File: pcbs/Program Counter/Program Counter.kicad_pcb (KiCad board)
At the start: 2 copper layers, 172.7 x 185.4 mm, 56 parts, among them J1001 Conn_02x20_Odd_Even, J1002 Conn_02x20_Odd_Even, U2001 74HC245, U2002 74HC245, U3001 74HC245, U3002 74HC245, U4001 74HC245, U4002 74HC245, U5001 74HC245, U5002 74HC245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

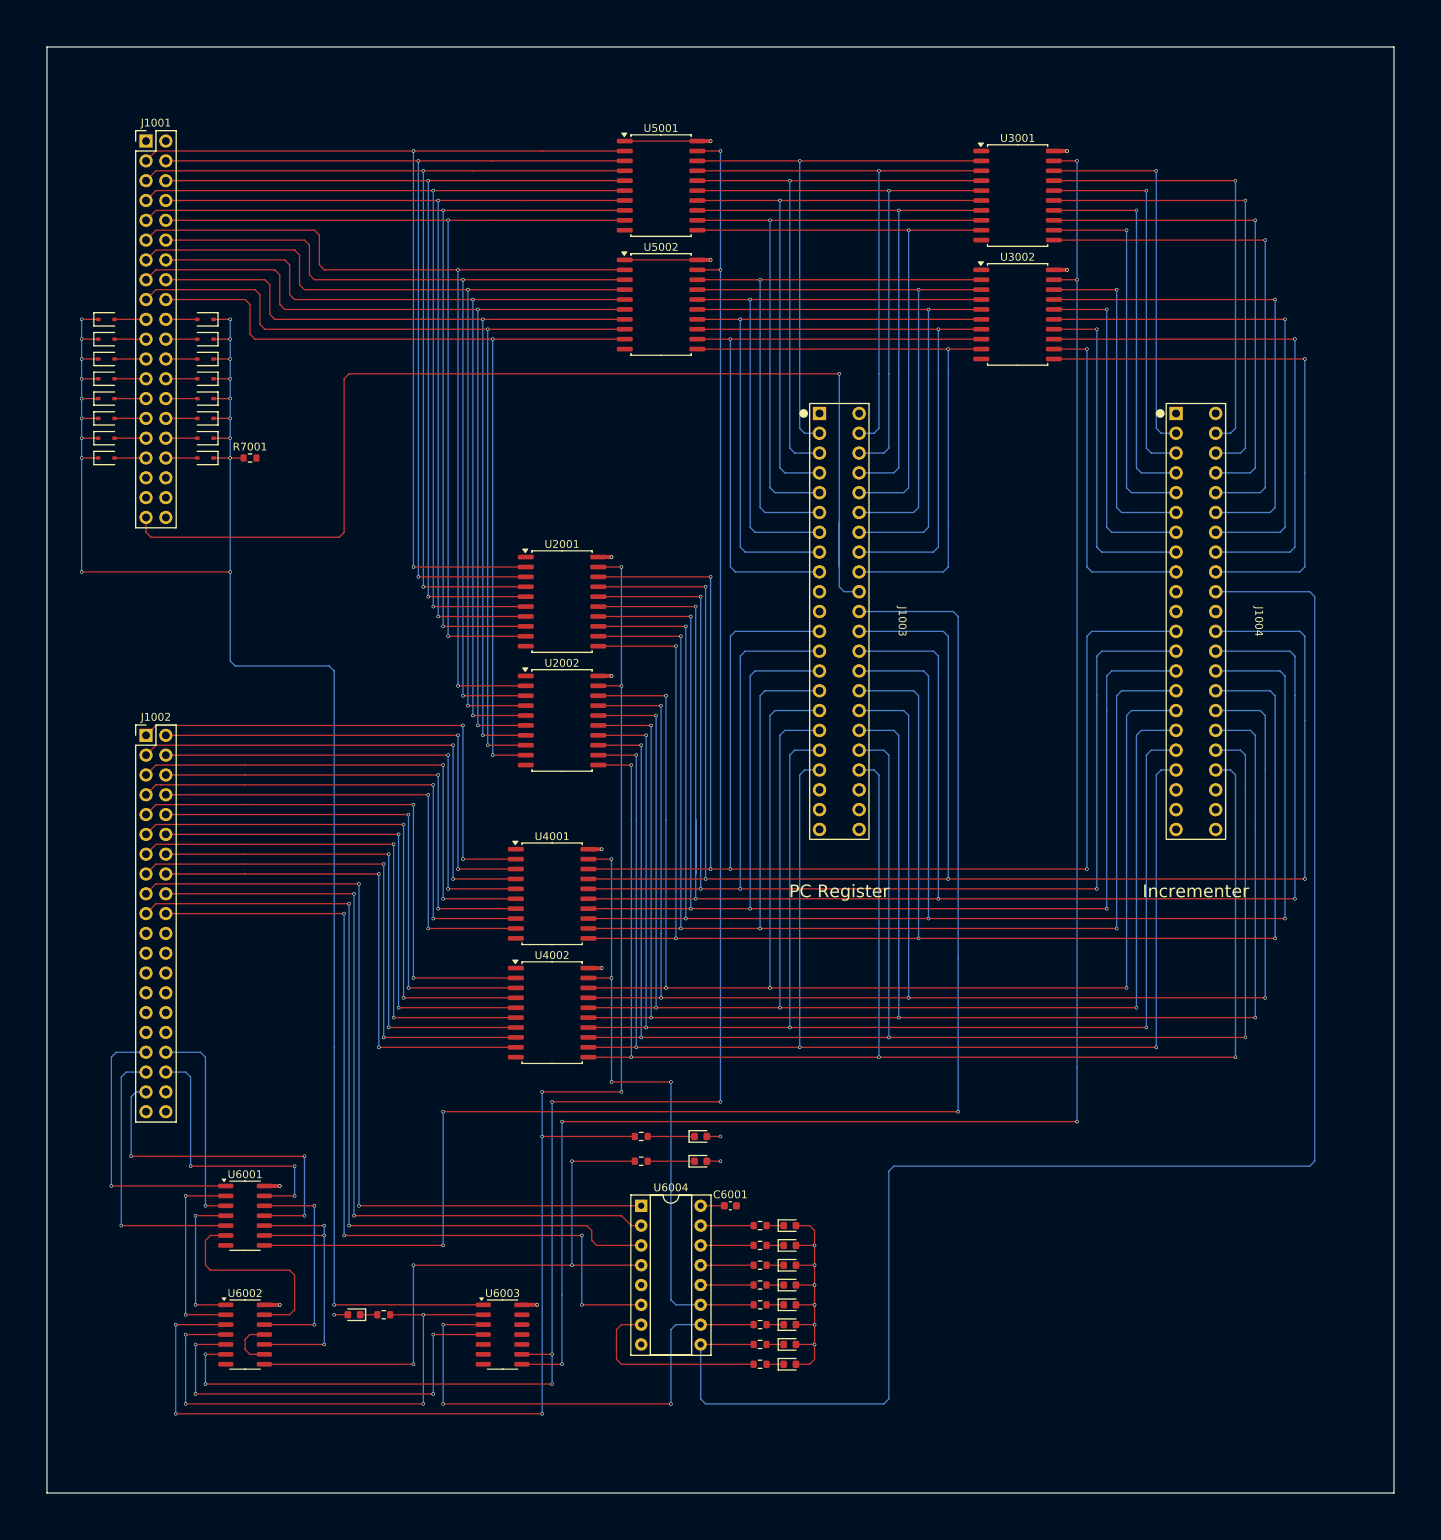
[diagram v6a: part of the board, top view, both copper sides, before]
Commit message: Some more LEDs and silkscreening
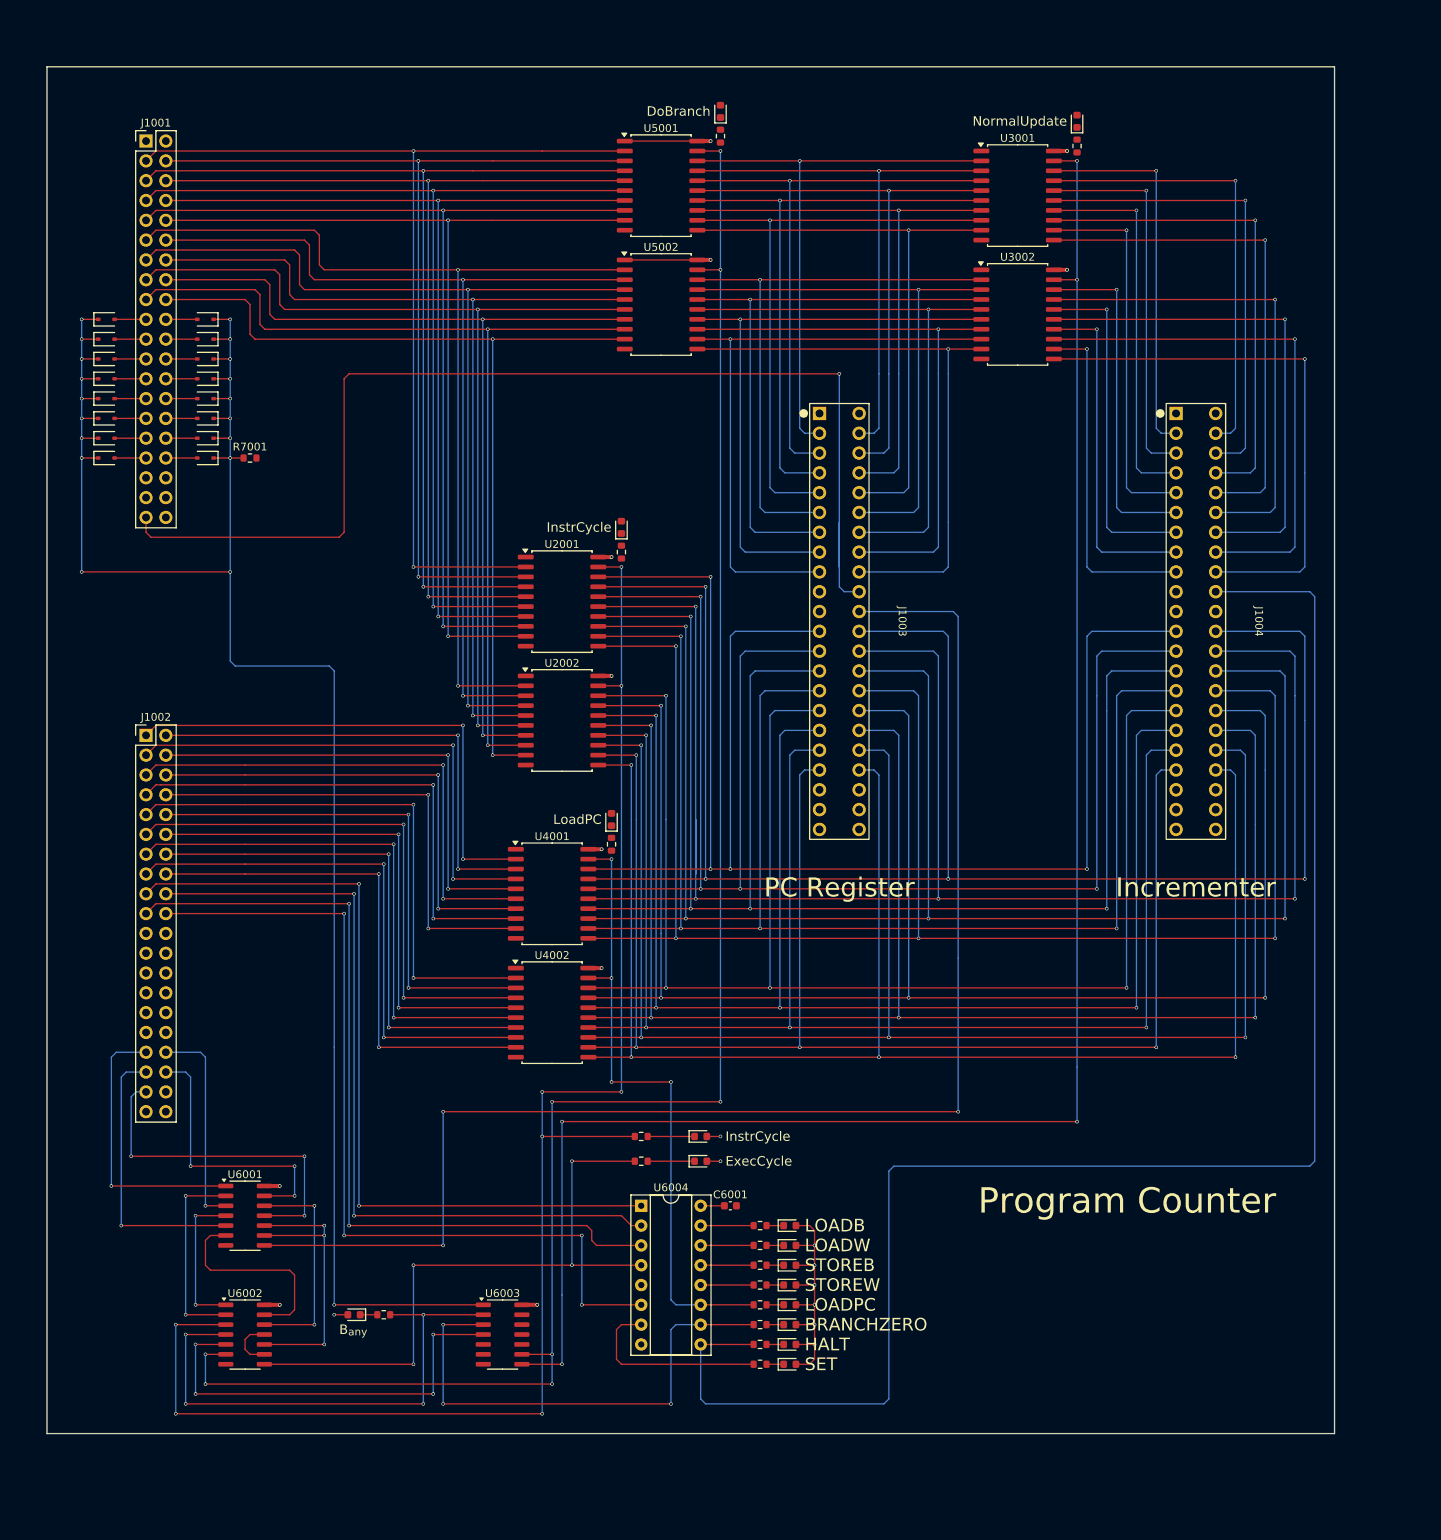
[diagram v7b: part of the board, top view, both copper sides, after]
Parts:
- added D2001: Blue, LED_SMD:LED_0603_1608Metric, F.Cu at (99.1, 89.5)
- added D3001: Blue, LED_SMD:LED_0603_1608Metric, F.Cu at (157.5, 37.5)
- added D4001: Blue, LED_SMD:LED_0603_1608Metric, F.Cu at (97.8, 127.0)
- added D5001: Blue, LED_SMD:LED_0603_1608Metric, F.Cu at (111.8, 36.2)
- added R2001: 4k7, Resistor_SMD:R_0603_1608Metric, F.Cu at (99.1, 92.7)
- added R3001: 4k7, Resistor_SMD:R_0603_1608Metric, F.Cu at (157.5, 40.6)
- added R4001: 4k7, Resistor_SMD:R_0603_1608Metric, F.Cu at (97.8, 130.2)
- added R5001: 4k7, Resistor_SMD:R_0603_1608Metric, F.Cu at (111.8, 39.4)
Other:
- board size 172.7 x 185.4 mm -> 165.1 x 175.3 mm
- board text added: "BRANCHZERO"
- board text added: "B_{any}"
- board text added: "DoBranch"
- board text added: "ExecCycle"
- board text added: "HALT"
- board text added: "InstrCycle"
- board text added: "LOADB"
- board text added: "LOADPC"
- board text added: "LOADW"
- board text added: "LoadPC"
- board text added: "NormalUpdate"
- board text added: "Program Counter"
- board text added: "SET"
- board text added: "STOREB"
- board text added: "STOREW"

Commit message: Prepping for final check
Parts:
- added H1001: MountingHole, MountingHole:MountingHole_2.7mm_M2.5_ISO7380, F.Cu at (30.5, 38.1)
- added H1002: MountingHole, MountingHole:MountingHole_2.7mm_M2.5_ISO7380, F.Cu at (30.5, 198.1)
- added H1003: MountingHole, MountingHole:MountingHole_2.7mm_M2.5_ISO7380, F.Cu at (182.9, 38.1)
- added H1004: MountingHole, MountingHole:MountingHole_2.7mm_M2.5_ISO7380, F.Cu at (182.9, 198.1)
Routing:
- net +5V: track 82.5 -> 87.0 mm, vias 20 -> 24
- net Net-(D5001-K): track 0.00 -> 1.56 mm
- net Net-(D4001-K): track 0.00 -> 1.56 mm
- net Net-(D3001-K): track 0.00 -> 1.56 mm
- net Net-(D2001-K): track 0.00 -> 1.56 mm
- net /~{LoadPC}: track 80.9 -> 82.0 mm
- net /~{NormalUpdate}: track 231.4 -> 232.5 mm
- net /~{InstrCycle}: track 201.4 -> 202.5 mm
- net /~{DoBranch}: track 240.4 -> 241.5 mm
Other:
- board size 165.1 x 175.3 mm -> 167.6 x 175.3 mm
- board text added: "+5V"
- board text added: "GND"
